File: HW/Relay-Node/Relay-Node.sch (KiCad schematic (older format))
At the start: 60 parts, among them IC1 STM8S003F3P, J1 CONN_01X04, J2 CONN_01X04, J3 CONN_01X04, J4 CONN_01X04, M1 NRF24L01, Q1 C1815, Q2 C1815, Q3 C1815, SW1 SW_Push, SW2 SW_Push, U1 ASM1117, U2 MC34063, U3 MAX485

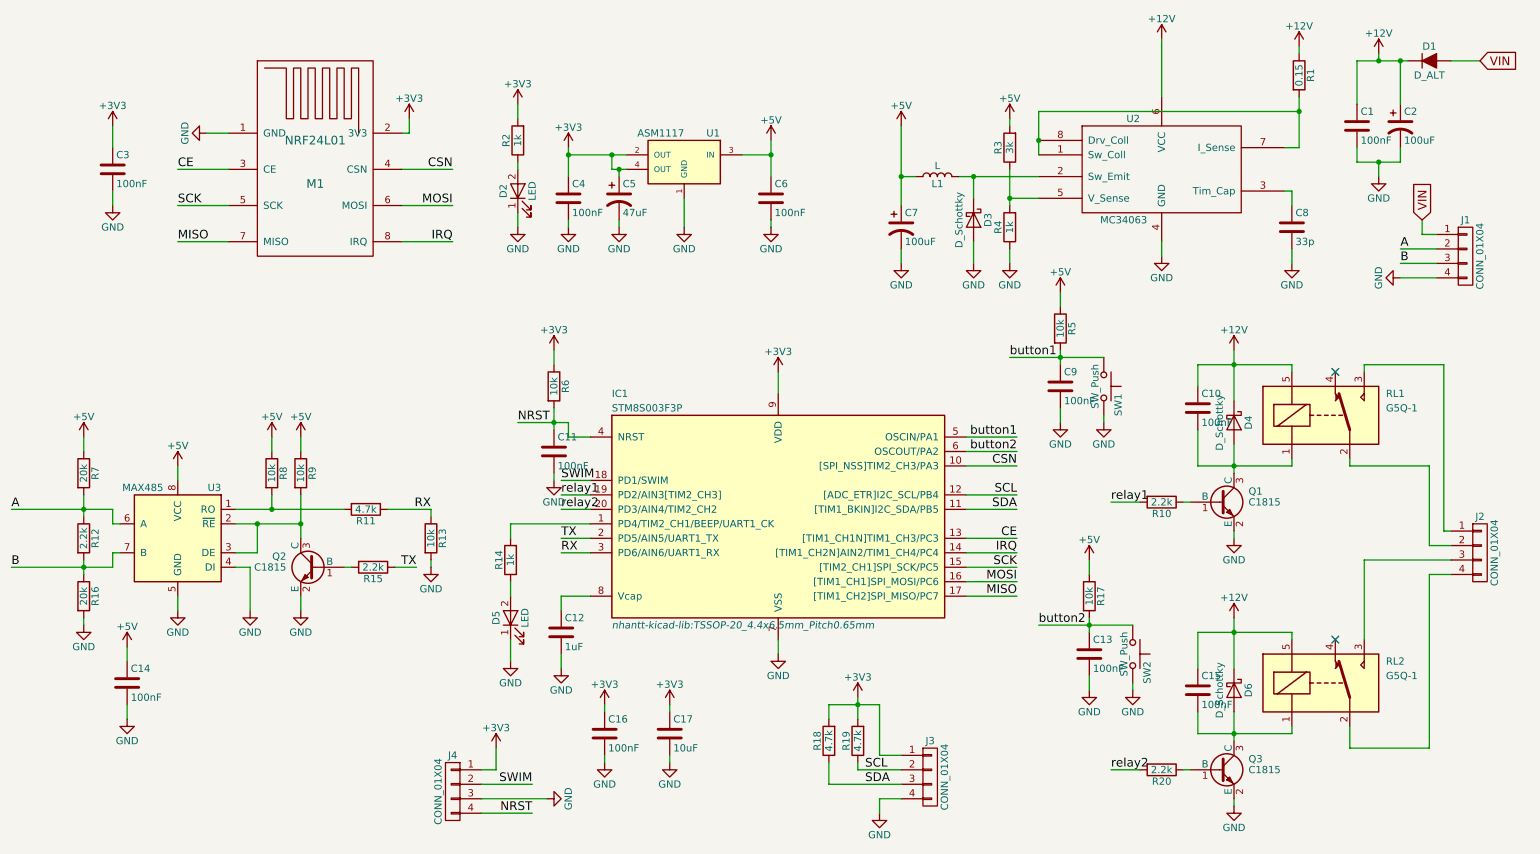
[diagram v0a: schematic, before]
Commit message: layout pcb relay-node
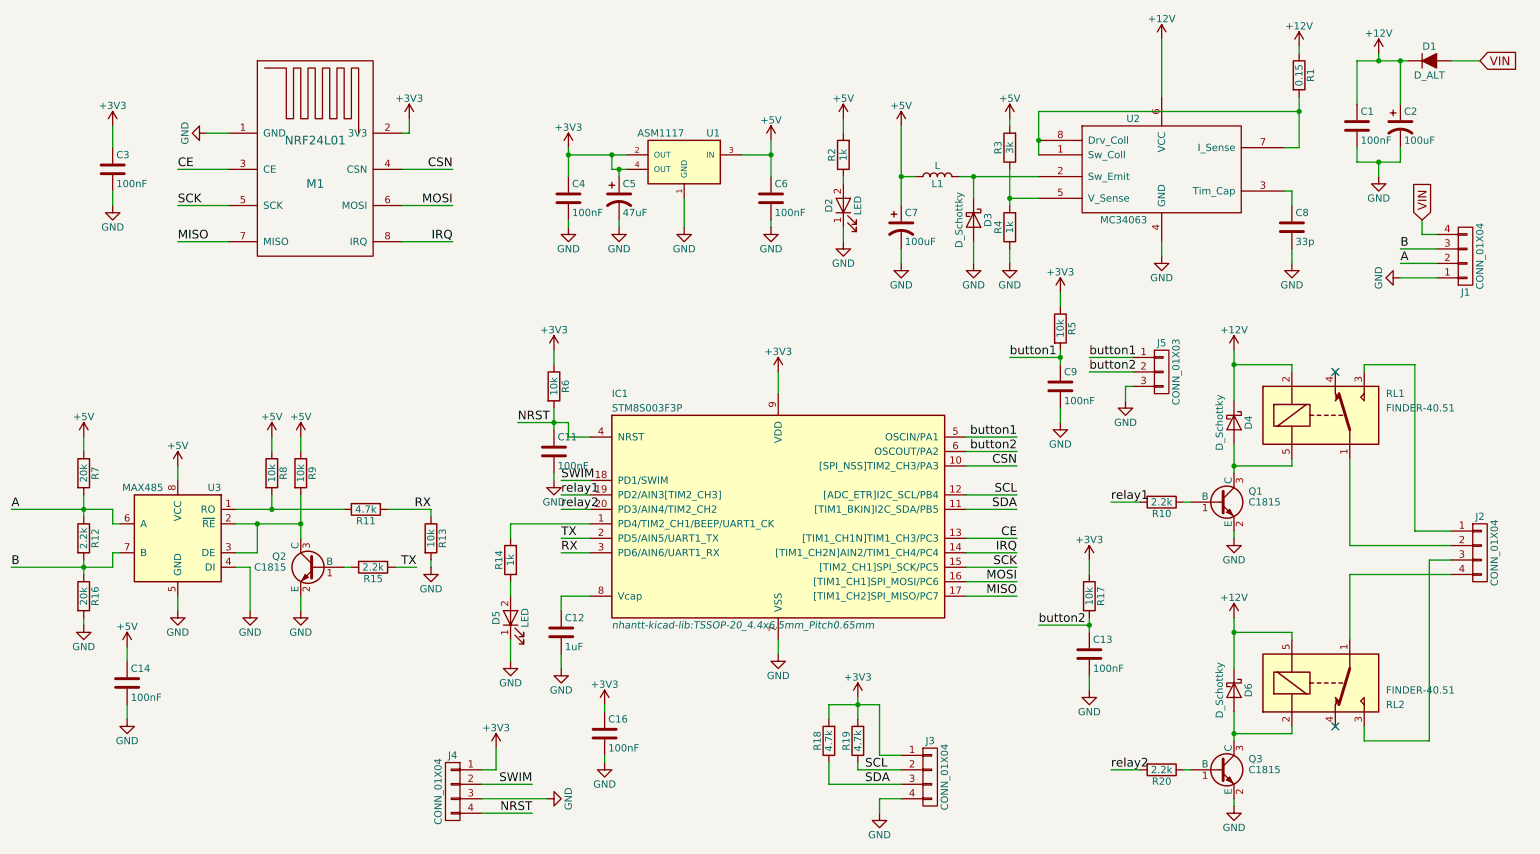
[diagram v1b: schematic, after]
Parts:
- removed C10, C15: 100nF, Capacitors_SMD:C_1206_HandSoldering, symbol C
- removed C17: 10uF, Resistors_SMD:R_1206_HandSoldering, symbol C
- removed RL1, RL2: G5Q-1, nhantt-kicad-lib:Relay_SRD-SONGLE, symbol G5Q-1
- removed SW1, SW2: SW_Push, nhantt-kicad-lib:Button-6mm-smd, symbol SW_Push
- added J5: CONN_01X03, nhantt-kicad-lib:Header-3pin-2.54, symbol CONN_01X03
- added RL1, RL2: FINDER-40.51, nhantt-kicad-lib:Relay_SRD-SONGLE, symbol FINDER-40.51
- J1, J2: footprint nhantt-kicad-lib:Terminal-3.81-4pin -> nhantt-kicad-lib:Domino-5.08mm_4pol
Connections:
- net +12V: now also RL1.2, RL2.5
- net +3V3: now also R17.1, R5.1; no longer R2.2
- net +5V: now also R2.2; no longer R17.1, R5.1
- net GND: now also J1.1 (P1), J5.3 (P3); no longer J1.4 (P4)
- net VIN: now also J1.4 (P4); no longer J1.1 (P1)
- net button1: now also J5.1 (P1)
- net button2: now also J5.2 (P2)
- net at D4.2 (A), Q1.3 (C): now also RL1.5
- net at J2.2 (P2): now also RL1.1
- net at J2.1 (P1): now also RL1.3
- net at D6.2 (A), Q3.3 (C): now also RL2.2
- net at J2.4 (P4): now also RL2.1
- net at J2.3 (P3): now also RL2.3
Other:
- moved on the sheet: D2, R2
